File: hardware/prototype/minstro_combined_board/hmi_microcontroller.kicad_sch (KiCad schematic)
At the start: 1 part, among them U201 ATSAMD10D13A-M

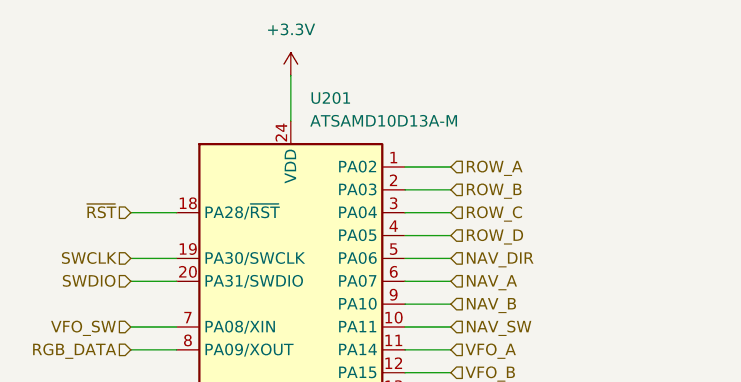
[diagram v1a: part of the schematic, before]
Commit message: Combined board started layout
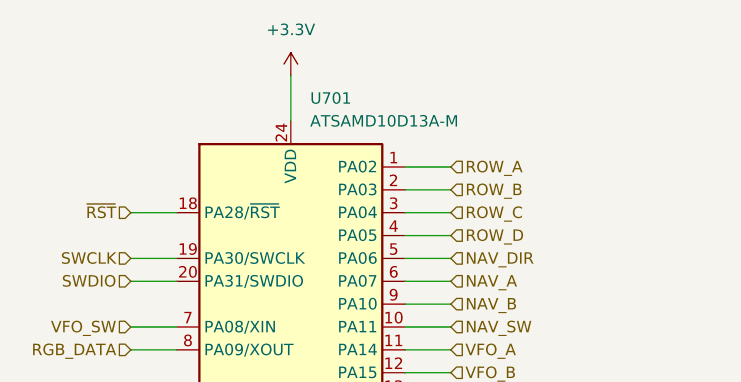
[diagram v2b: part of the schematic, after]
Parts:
- renumbered U201 to U701
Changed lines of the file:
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@@
 		(dnp no)
 		(fields_autoplaced yes)
-		(property "Reference" "#PWR0201"
+		(property "Reference" "#PWR0701"
 			(at 66.04 77.47 0)
 			(effects
@@
 			(project ""
 				(path "/edc2d64f-9cdb-4ab0-b2de-c3cfa55e1c10/e7d7ed5c-7a0d-40e5-948b-719d08b13ce9"
-					(reference "#PWR0201")
+					(reference "#PWR0701")
 					(unit 1)
 				)
@@
 		(dnp no)
 		(fields_autoplaced yes)
-		(property "Reference" "#PWR0202"
+		(property "Reference" "#PWR0702"
 			(at 66.04 139.7 0)
 			(effects
@@
 			(project ""
 				(path "/edc2d64f-9cdb-4ab0-b2de-c3cfa55e1c10/e7d7ed5c-7a0d-40e5-948b-719d08b13ce9"
-					(reference "#PWR0202")
+					(reference "#PWR0702")
 					(unit 1)
 				)
@@
 		(dnp no)
 		(fields_autoplaced yes)
-		(property "Reference" "U201"
+		(property "Reference" "U701"
 			(at 68.1833 76.2 0)
 			(effects
@@
 			(project "hmi_board"
 				(path "/edc2d64f-9cdb-4ab0-b2de-c3cfa55e1c10/e7d7ed5c-7a0d-40e5-948b-719d08b13ce9"
-					(reference "U201")
-					(unit 1)
-				)
+					(reference "U701")
+					(unit 1)
+				)

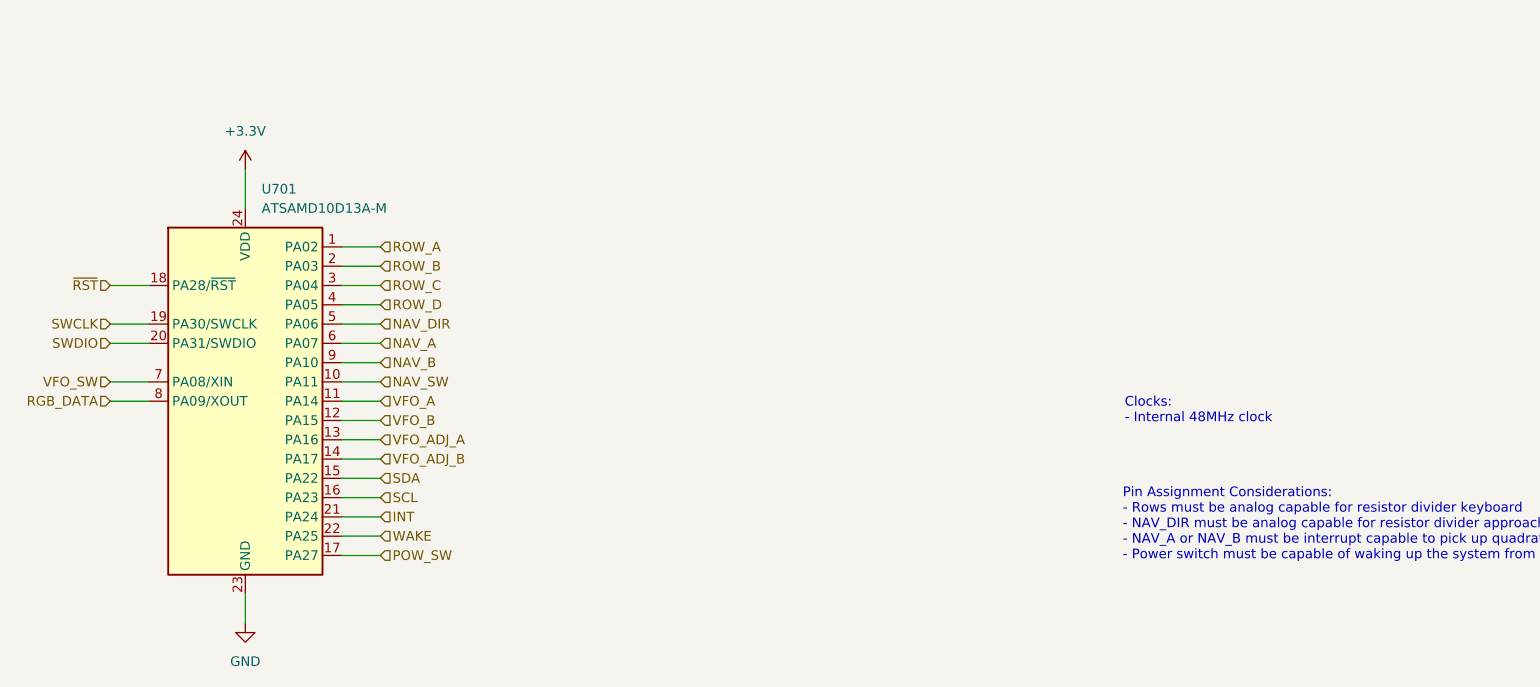
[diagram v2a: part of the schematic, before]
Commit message: Schematic ERC complete
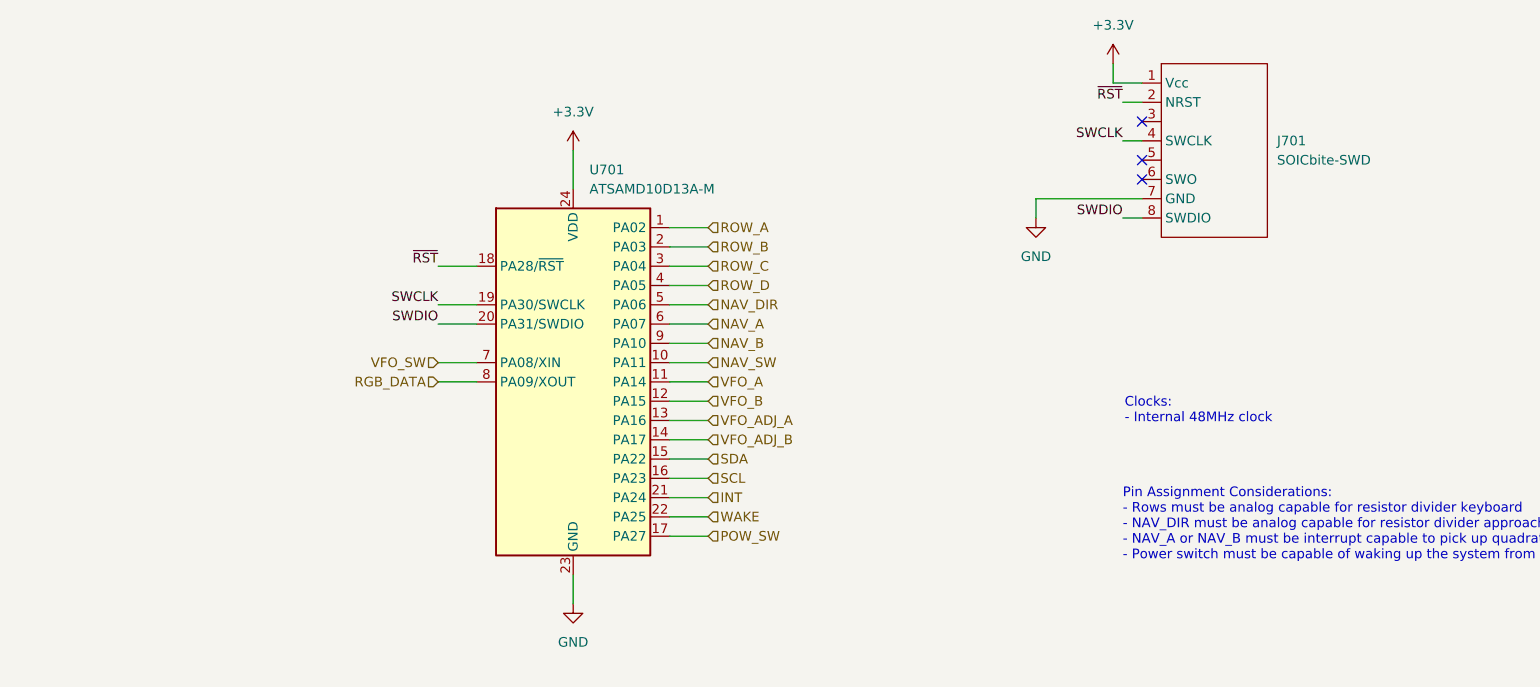
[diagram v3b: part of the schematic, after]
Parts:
- added J701: SOICbite-SWD, BVH_SOICbite:SOICbite_renumbered, symbol BVH_SOICbite:SOICbite-SWD
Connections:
- net +3.3V: now also J701.1 (Vcc)
- net GND: now also J701.7 (GND)
- net SWCLK: now also J701.4 (SWCLK)
- net SWDIO: now also J701.8 (SWDIO)
- net ~{RST}: now also J701.2 (NRST)
- no-connect marks 0 -> 3
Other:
- moved on the sheet: U701

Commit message: Layout and routing Power and initial signals, SD card
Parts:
- added C701: 10uF, Capacitor_SMD:C_0805_2012Metric, symbol Device:C_Small
- added C702, C703: 0.1uF, Capacitor_SMD:C_0603_1608Metric, symbol Device:C_Small
- added JP701: Jumper_2_Open, Jumper:SolderJumper-2_P1.3mm_Open_Pad1.0x1.5mm, symbol Jumper:Jumper_2_Open
- added Q701: 2N7002, Package_TO_SOT_SMD:SOT-23, symbol Transistor_FET:2N7002
- added R701, R702: 10k, Resistor_SMD:R_0805_2012Metric_Pad1.20x1.40mm_HandSolder, symbol Device:R_Small
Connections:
- net ROW_D is gone; now on net ROW_A: U701.4 (PA05)
- net +3.3V: now also C701.1, C702.1, C703.1, Q701.1 (G), R701.2
- net GND: now also C701.2, C702.2, C703.2
- net RGB_DATA: now also JP701.2 (B), Q701.3 (D), R702.2; no longer U701.8 (PA09/XOUT)
- net ROW_A: no longer U701.1 (PA02)
- net ROW_C: now also U701.1 (PA02); no longer U701.3 (PA04)
- new net +5V: R702.1
- new net RGB_DATA_3.3: JP701.1 (A), Q701.2 (S), R701.1, U701.8 (PA09/XOUT)
- no-connect marks 3 -> 4
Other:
- note added: "LED Data Level Shifter DNP and Close JP101 for 3.3V logic to LEDs"

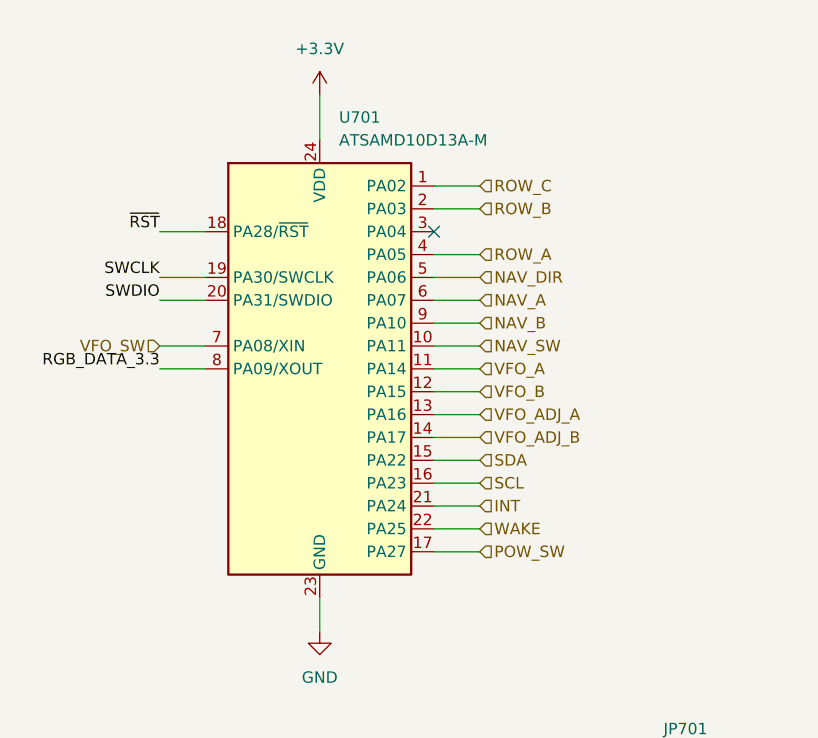
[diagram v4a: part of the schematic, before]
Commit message: Board resizing
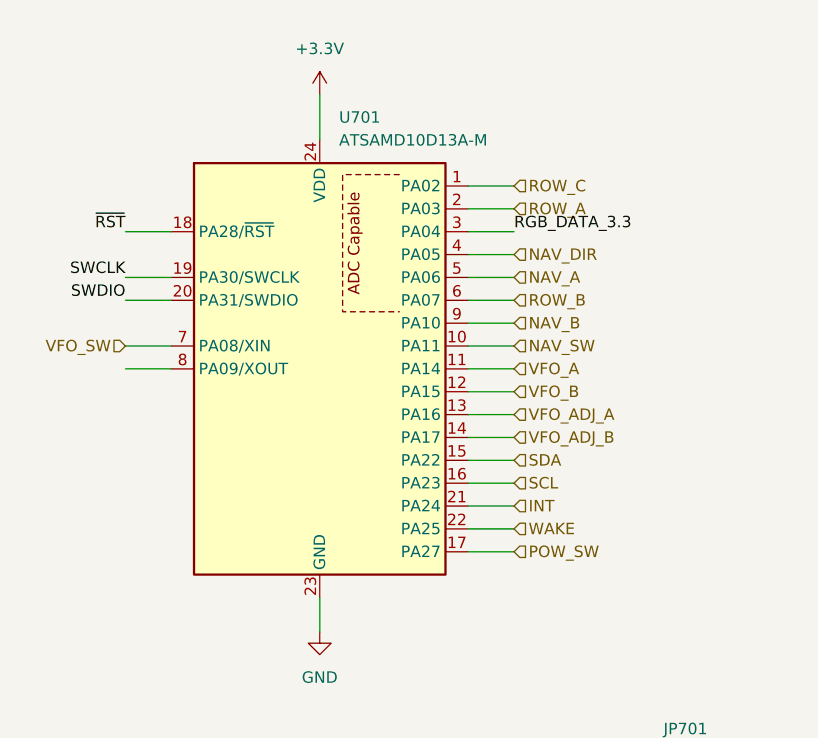
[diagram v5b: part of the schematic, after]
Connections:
- net NAV_A: now also U701.5 (PA06); no longer U701.6 (PA07)
- net NAV_DIR: now also U701.4 (PA05); no longer U701.5 (PA06)
- net RGB_DATA_3.3: now also U701.3 (PA04); no longer U701.8 (PA09/XOUT)
- net ROW_A: now also U701.2 (PA03); no longer U701.4 (PA05)
- net ROW_B: now also U701.6 (PA07); no longer U701.2 (PA03)
- no-connect marks 4 -> 3
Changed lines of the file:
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@@
-	)
-	(no_connect
-		(at 121.92 86.36)
 	)
 	(no_connect
@@
 	(wire
 		(pts
-			(xy 91.44 99.06) (xy 96.52 99.06)
+			(xy 87.63 99.06) (xy 92.71 99.06)
 		)
 		(stroke
@@
 	(wire
 		(pts
-			(xy 91.44 101.6) (xy 96.52 101.6)
+			(xy 87.63 101.6) (xy 92.71 101.6)
 		)
 		(stroke
@@
 	(wire
 		(pts
-			(xy 121.92 119.38) (xy 127 119.38)
+			(xy 125.73 119.38) (xy 130.81 119.38)
 		)
 		(stroke
@@
 	(wire
 		(pts
-			(xy 121.92 106.68) (xy 127 106.68)
-		)
-		(stroke
-			(width 0)
-			(type default)
-		)
-	)
-	(wire
-		(pts
-			(xy 121.92 99.06) (xy 127 99.06)
+			(xy 125.73 106.68) (xy 130.81 106.68)
+		)
+		(stroke
+			(width 0)
+			(type default)
+		)
+	)
+	(wire
+		(pts
+			(xy 125.73 99.06) (xy 130.81 99.06)
 		)
 		(stroke
@@
 	(wire
 		(pts
-			(xy 91.44 91.44) (xy 96.52 91.44)
+			(xy 87.63 91.44) (xy 92.71 91.44)
 		)
 		(stroke
@@
 	(wire
 		(pts
-			(xy 91.44 93.98) (xy 96.52 93.98)
+			(xy 87.63 93.98) (xy 92.71 93.98)
 		)
 		(stroke
@@
 	(wire
 		(pts
-			(xy 121.92 83.82) (xy 127 83.82)
-		)
-		(stroke
-			(width 0)
-			(type default)
-		)
-	)
-	(wire
-		(pts
-			(xy 121.92 116.84) (xy 127 116.84)
-		)
-		(stroke
-			(width 0)
-			(type default)
-		)
-	)
-	(wire
-		(pts
-			(xy 121.92 96.52) (xy 127 96.52)
+			(xy 125.73 86.36) (xy 130.81 86.36)
+		)
+		(stroke
+			(width 0)
+			(type default)
+		)
+	)
+	(wire
+		(pts
+			(xy 125.73 83.82) (xy 130.81 83.82)
+		)
+		(stroke
+			(width 0)
+			(type default)
+		)
+	)
+	(wire
+		(pts
+			(xy 125.73 116.84) (xy 130.81 116.84)
+		)
+		(stroke
+			(width 0)
+			(type default)
+		)
+	)
+	(wire
+		(pts
+			(xy 125.73 96.52) (xy 130.81 96.52)
 		)
 		(stroke
@@
 	(wire
 		(pts
-			(xy 121.92 109.22) (xy 127 109.22)
+			(xy 125.73 109.22) (xy 130.81 109.22)
 		)
 		(stroke
@@
 	(wire
 		(pts
-			(xy 121.92 91.44) (xy 127 91.44)
+			(xy 125.73 91.44) (xy 130.81 91.44)
 		)
 		(stroke
@@
 	(wire
 		(pts
-			(xy 121.92 104.14) (xy 127 104.14)
-		)
-		(stroke
-			(width 0)
-			(type default)
-		)
-	)
-	(wire
-		(pts
-			(xy 121.92 101.6) (xy 127 101.6)
-		)
-		(stroke
-			(width 0)
-			(type default)
-		)
-	)
-	(wire
-		(pts
-			(xy 121.92 88.9) (xy 127 88.9)
+			(xy 125.73 104.14) (xy 130.81 104.14)
+		)
+		(stroke
+			(width 0)
+			(type default)
+		)
+	)
+	(wire
+		(pts
+			(xy 125.73 101.6) (xy 130.81 101.6)
+		)
+		(stroke
+			(width 0)
+			(type default)
+		)
+	)
+	(wire
+		(pts
+			(xy 125.73 88.9) (xy 130.81 88.9)
 		)
 		(stroke
@@
 	(wire
 		(pts
-			(xy 91.44 86.36) (xy 96.52 86.36)
+			(xy 87.63 86.36) (xy 92.71 86.36)
 		)
 		(stroke
@@
 	(wire
 		(pts
-			(xy 121.92 121.92) (xy 127 121.92)
+			(xy 125.73 121.92) (xy 130.81 121.92)
 		)
 		(stroke
@@
 	(wire
 		(pts
-			(xy 121.92 93.98) (xy 127 93.98)
-		)
-		(stroke
-			(width 0)
-			(type default)
-		)
-	)
-	(wire
-		(pts
-			(xy 121.92 81.28) (xy 127 81.28)
+			(xy 125.73 93.98) (xy 130.81 93.98)
+		)
+		(stroke
+			(width 0)
+			(type default)
+		)
+	)
+	(wire
+		(pts
+			(xy 125.73 81.28) (xy 130.81 81.28)
 		)
 		(stroke
@@
 	(wire
 		(pts
-			(xy 121.92 114.3) (xy 127 114.3)
-		)
-		(stroke
-			(width 0)
-			(type default)
-		)
-	)
-	(wire
-		(pts
-			(xy 121.92 111.76) (xy 127 111.76)
+			(xy 125.73 114.3) (xy 130.81 114.3)
+		)
+		(stroke
+			(width 0)
+			(type default)
+		)
+	)
+	(wire
+		(pts
+			(xy 125.73 111.76) (xy 130.81 111.76)
 		)
 		(stroke
@@
 	)
 	(label "SWDIO"
-		(at 91.44 93.98 180)
+		(at 87.63 93.98 180)
 		(effects
 			(font
@@
 	)
 	(label "SWCLK"
-		(at 91.44 91.44 180)
+		(at 87.63 91.44 180)
 		(effects
 			(font
@@
 	)
 	(label "~{RST}"
-		(at 91.44 86.36 180)
+		(at 87.63 86.36 180)
 		(effects
 			(font
@@
 	)
 	(label "RGB_DATA_3.3"
-		(at 91.44 101.6 180)
-		(effects
-			(font
-				(size 1.27 1.27)
-			)
-			(justify right bottom)
+		(at 130.81 86.36 0)
+		(effects
+			(font
+				(size 1.27 1.27)
+			)
+			(justify left bottom)
 		)
 	)
@@
 	(hierarchical_label "ROW_B"
 		(shape input)
-		(at 127 83.82 0)
+		(at 130.81 93.98 0)
 		(effects
 			(font
@@
 	(hierarchical_label "WAKE"
 		(shape input)
-		(at 127 119.38 0)
+		(at 130.81 119.38 0)
 		(effects
 			(font
@@
 	(hierarchical_label "VFO_B"
 		(shape input)
-		(at 127 104.14 0)
+		(at 130.81 104.14 0)
 		(effects
 			(font
@@
 	(hierarchical_label "SCL"
 		(shape input)
-		(at 127 114.3 0)
+		(at 130.81 114.3 0)
 		(effects
 			(font
@@
 	(hierarchical_label "SDA"
 		(shape input)
-		(at 127 111.76 0)
+		(at 130.81 111.76 0)
 		(effects
 			(font
@@
 	(hierarchical_label "INT"
 		(shape input)
-		(at 127 116.84 0)
+		(at 130.81 116.84 0)
 		(effects
 			(font
@@
 	(hierarchical_label "VFO_A"
 		(shape input)
-		(at 127 101.6 0)
+		(at 130.81 101.6 0)
 		(effects
 			(font
@@
 	(hierarchical_label "NAV_A"
 		(shape input)
-		(at 127 93.98 0)
+		(at 130.81 91.44 0)
 		(effects
 			(font
@@
 	(hierarchical_label "VFO_ADJ_B"
 		(shape input)
-		(at 127 109.22 0)
+		(at 130.81 109.22 0)
 		(effects
 			(font
@@
 	(hierarchical_label "POW_SW"
 		(shape input)
-		(at 127 121.92 0)
+		(at 130.81 121.92 0)
 		(effects
 			(font
@@
 	(hierarchical_label "ROW_C"
 		(shape input)
-		(at 127 81.28 0)
+		(at 130.81 81.28 0)
 		(effects
 			(font
@@
 	(hierarchical_label "NAV_B"
 		(shape input)
-		(at 127 96.52 0)
+		(at 130.81 96.52 0)
 		(effects
 			(font
@@
 	(hierarchical_label "NAV_DIR"
 		(shape input)
-		(at 127 91.44 0)
+		(at 130.81 88.9 0)
 		(effects
 			(font
@@
 	(hierarchical_label "ROW_A"
 		(shape input)
-		(at 127 88.9 0)
+		(at 130.81 83.82 0)
 		(effects
 			(font
@@
 	(hierarchical_label "VFO_SW"
 		(shape input)
-		(at 91.44 99.06 180)
+		(at 87.63 99.06 180)
 		(effects
 			(font
@@
 	(hierarchical_label "VFO_ADJ_A"
 		(shape input)
-		(at 127 106.68 0)
+		(at 130.81 106.68 0)
 		(effects
 			(font
@@
 	(hierarchical_label "NAV_SW"
 		(shape input)
-		(at 127 99.06 0)
-		(effects
-			(font
+		(at 130.81 99.06 0)
+		(effects
+			(font

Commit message: Layout completed, initial review
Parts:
- added J702: Conn_ARM_JTAG_SWD_10, BVH_Connectors_Misc:Cortex_Debug_PinSocket_2x05_P1.27mm_Vertical_SMD, symbol Connector:Conn_ARM_JTAG_SWD_10
- U701: footprint Package_DFN_QFN:QFN-24-1EP_4x4mm_P0.5mm_EP2.6x2.6mm -> Package_DFN_QFN:QFN-24-1EP_4x4mm_P0.5mm_EP2.6x2.6mm_ThermalVias
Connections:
- net +3.3V: now also J702.1 (VTref)
- net GND: now also J702.3 (GND), J702.5 (GND), J702.9 (GNDDetect)
- net SWCLK: now also J702.4 (SWCLK/TCK)
- net SWDIO: now also J702.2 (SWDIO/TMS)
- net ~{RST}: now also J702.10 (~{RESET})
- no-connect marks 3 -> 6

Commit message: HMI processor firmware started
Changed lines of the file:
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@@
 				(size 1.27 1.27)
 			)
-			(justify right)
+			(justify left)
 		)
 	)
